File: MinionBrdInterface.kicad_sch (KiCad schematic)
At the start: 28 parts, among them J4 Dashboard, J6 Display, Q5 IRLML0030, Q6 IRLML0030, U2 EL3H7, U23 EL3H7, U24 EL3H7, U27 EL3H7, U28 EL3H7, U29 EL3H7, U4 EL3H7, U5 EL3H7

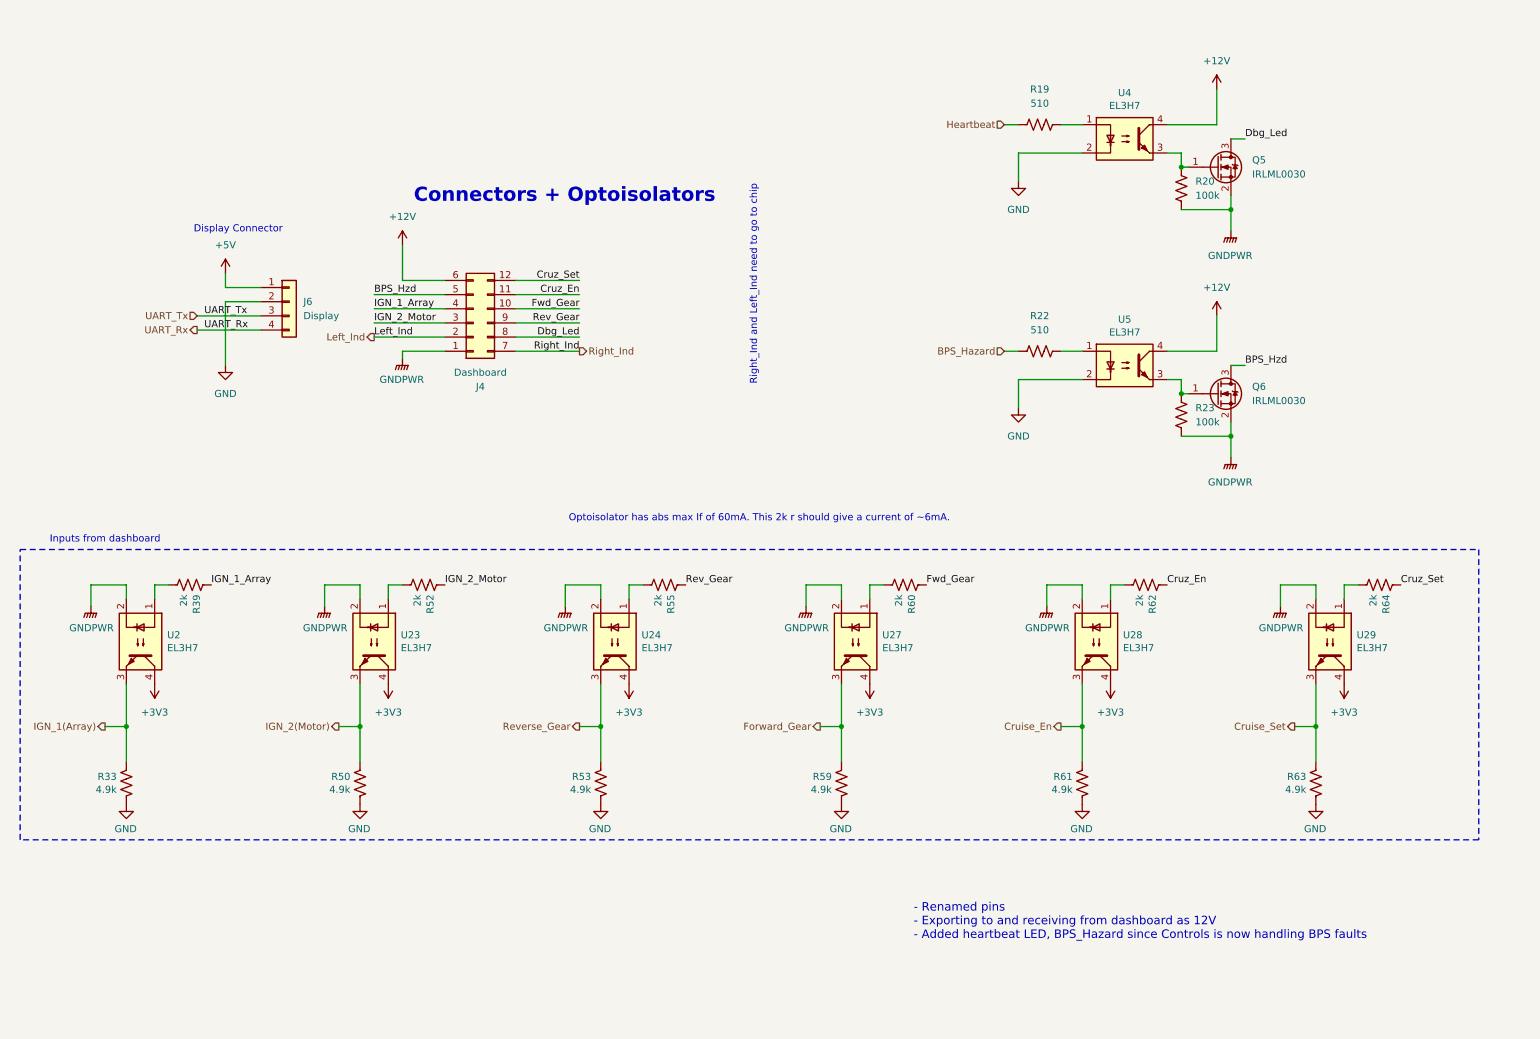
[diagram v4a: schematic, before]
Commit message: Removed precharge contactor stuff, made accel 5V instead of 3, removed op amp for brake.
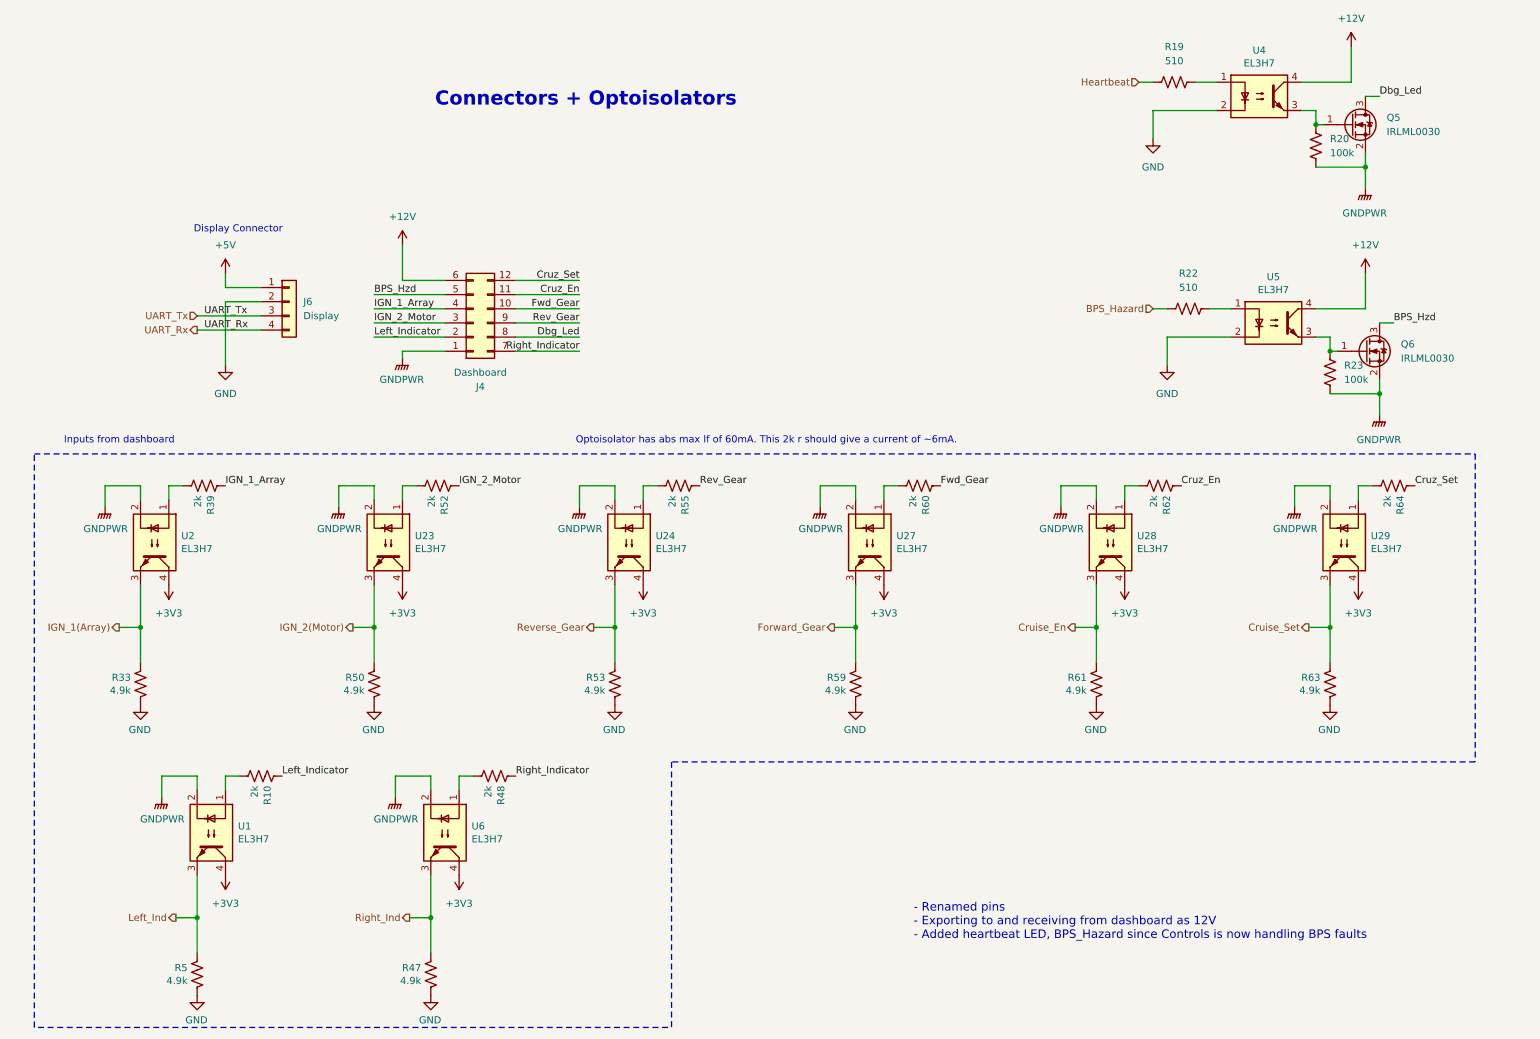
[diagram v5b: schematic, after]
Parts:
- added R10, R48: 2k, Resistor_SMD:R_0805_2012Metric, symbol Device:R_US
- added R47, R5: 4.9k, Resistor_SMD:R_0805_2012Metric, symbol Device:R_US
- added U1, U6: EL3H7, Package_SO:SSOP-4_4.4x2.6mm_P1.27mm, symbol Isolator:SFH617A-1
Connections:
- net +3V3: now also U1.4, U6.4
- net GND: now also R47.2, R5.2
- net GNDPWR: now also U1.2, U6.2
- net Left_Ind: now also R5.1, U1.3; no longer J4.2 (Pin_2)
- net Right_Ind: now also R47.1, U6.3; no longer J4.7 (Pin_7)
- new net: R10.2, U1.1
- new net: R48.2, U6.1
- new net Left_Indicator: J4.2 (Pin_2), R10.1
- new net Right_Indicator: J4.7 (Pin_7), R48.1
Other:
- note removed: "Right_Ind and Left_Ind need to go to chip"
- moved on the sheet: Q5, Q6, R19, R20, R22, R23, R33, R39, R50, R52, R53, R55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

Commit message: Added part numbers wheeeeeeeeeeeeeeeeeeeee
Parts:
- Q5, Q6: JLCPCB# (none) -> C5364304
- R10, R39, R48, R52, R55, R60, R62, R64: JLCPCB# (none) -> C17604
- R19, R22: JLCPCB# (none) -> C17734
- R20, R23: JLCPCB# (none) -> C149504
- R33, R47, R5, R50, R53, R59, R61, R63: JLCPCB# (none) -> C27834
- U1, U2, U23, U24, U27, U28, U29, U4, U5, U6: JLCPCB# (none) -> C32565

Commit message: Change schottky diode footprint, update JLCPcB parts.
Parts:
- Q5, Q6: JLCPCB# C5364304 -> C67272
- U1, U2, U23, U24, U27, U28, U29, U4, U5, U6: JLCPCB# C32565 -> C92243
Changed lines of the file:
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@@
 			)
 		)
-		(property "JLCPCB#" "C32565"
+		(property "JLCPCB#" "C92243"
 			(at 242.57 69.85 0)
 			(effects
@@
 			)
 		)
-		(property "JLCPCB#" "C32565"
+		(property "JLCPCB#" "C92243"
 			(at 52.07 161.29 0)
 			(effects
@@
 			)
 		)
-		(property "JLCPCB#" "C32565"
+		(property "JLCPCB#" "C92243"
 			(at 170.18 109.22 0)
 			(effects
@@
 			)
 		)
-		(property "JLCPCB#" "C32565"
+		(property "JLCPCB#" "C92243"
 			(at 127 109.22 0)
 			(effects
@@
 			)
 		)
-		(property "JLCPCB#" "C32565"
+		(property "JLCPCB#" "C92243"
 			(at 240.03 29.21 0)
 			(effects
@@
 			)
 		)
-		(property "JLCPCB#" "C32565"
+		(property "JLCPCB#" "C92243"
 			(at 255.27 109.22 0)
 			(effects
@@
 			)
 		)
-		(property "JLCPCB#" "C32565"
+		(property "JLCPCB#" "C92243"
 			(at 41.91 109.22 0)
 			(effects
@@
 			)
 		)
-		(property "JLCPCB#" "C5364304"
+		(property "JLCPCB#" "C67272"
 			(at 256.54 34.29 0)
 			(effects
@@
 			)
 		)
-		(property "JLCPCB#" "C32565"
+		(property "JLCPCB#" "C92243"
 			(at 93.98 161.29 0)
 			(effects
@@
 			)
 		)
-		(property "JLCPCB#" "C32565"
+		(property "JLCPCB#" "C92243"
 			(at 83.82 109.22 0)
 			(effects
@@
 			)
 		)
-		(property "JLCPCB#" "C5364304"
+		(property "JLCPCB#" "C67272"
 			(at 259.08 74.93 0)
 			(effects
@@
 			)
 		)
-		(property "JLCPCB#" "C32565"
+		(property "JLCPCB#" "C92243"
 			(at 213.36 109.22 0)
 			(effects
